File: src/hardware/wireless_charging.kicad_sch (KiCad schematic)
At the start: 0 parts

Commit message: Added Wireless Charging
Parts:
- added C? (x4): 22nF, symbol Device:C
- added C? (x2): 470nF, symbol Device:C
- added C?: 100pF, symbol Device:C
- added C? (x3): 10nF, symbol Device:C
- added C? (x2): 100nF, symbol Device:C
- added C?: 2.2nF, symbol Device:C
- added C?: 10µF, symbol Device:C
- added L?: WE-WPCC_RX_1COIL, WE-WPCC_RX_1COIL:WE-WPCC_RX_760308103205, symbol WE-WPCC_RX_1COIL:WE-WPCC_RX_1COIL
- added Q? (x2): Q_NMOS, symbol Device:Q_NMOS
- added R?: 422, symbol Device:R
- added R?: 1.5k, symbol Device:R
- added R?: 200, symbol Device:R
- added R?: 10k, symbol Device:R
- added U?: BQ51013BRHLR, BQ51013BRHLR:IC_MSP430FR2522IRHLR, symbol BQ51013BRHLR:BQ51013BRHLR
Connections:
- new net: C?.2, C?.2, C?.2, C?.2, L?.1
- new net: R?.1, U?.12 (ILIM)
- new net: R?.1, R?.2, U?.14 (FOD)
- new net: Q?.D, Q?.D
- new net: R?.1, U?.7 (~{CHG})
- new net: R?.1, U?.13 (TS/CTRL)
- new net AC1: C?.1, C?.1, C?.1, C?.1, C?.1, C?.1, C?.2, C?.2, C?.2, U?.2 (AC1)
- new net AC2: C?.2, C?.2, C?.2, C?.2, C?.2, L?.2, U?.18 (RECT), U?.19 (AC2)
- new net BOOT1: C?.1, U?.3 (BOOT1)
- new net BOOT2: C?.1, U?.17 (BOOT2)
- new net CLAMP1: C?.1, U?.5 (CLAMP1)
- new net CLAMP2: C?.1, U?.16 (CLAMP2)
- new net COMM1: C?.1, U?.6 (COMM1)
- new net COMM2: C?.1, U?.15 (COMM2)
- new net EXP: C?.1, C?.1, R?.2, R?.2, U?.1 (PGND), U?.10 (EN1), U?.11 (EN2), U?.20 (PGND), U?.21 (EXP), U?.22 (EXP), U?.23 (EXP), U?.24 (EXP), U?.25 (EXP), U?.26 (EXP), U?.27 (EXP), U?.28 (EXP), U?.29 (EXP)
- new net SOLAR: C?.2, C?.2, Q?.S, U?.9 (AD)
- new net WCDET: R?.2
- new net \ADEN: Q?.G, Q?.G, U?.8 (~{AD}-EN)

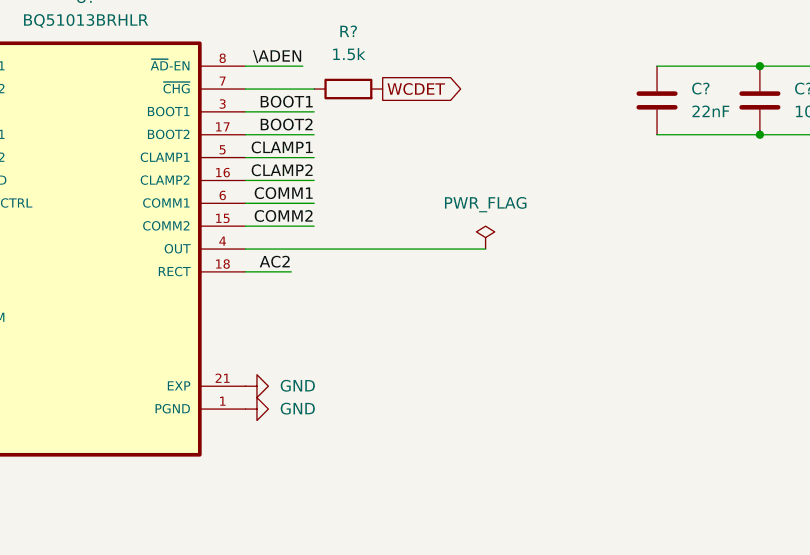
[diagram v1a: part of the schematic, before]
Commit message: Fixed Wireless Charging
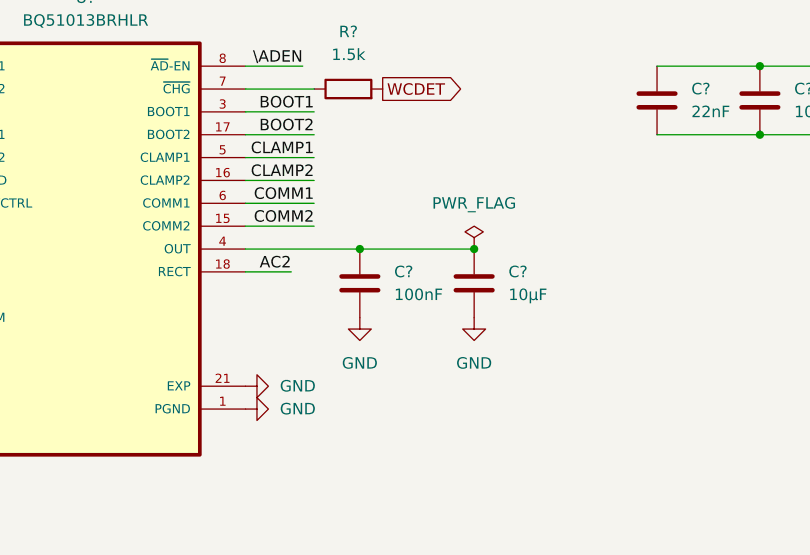
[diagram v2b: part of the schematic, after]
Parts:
- added C?: 100nF, symbol Device:C
- added C?: 10µF, symbol Device:C
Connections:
- net EXP: now also C?.2, C?.2
- net at U?.4 (OUT): now also C?.1, C?.1

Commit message: Added Solar Status
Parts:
- added R6: 10k, symbol Device:R
- R?: value 1.5k -> 10k
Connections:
- net \ADEN: now also R6.1
- new net SOLARSTAT: R6.2
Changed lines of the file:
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@@
+	)
+	(junction
+		(at 161.29 76.2)
+		(diameter 0)
+		(color 0 0 0 0)
 	)
 	(junction
@@
 	(wire
 		(pts
+			(xy 161.29 67.31) (xy 161.29 76.2)
+		)
+		(stroke
+			(width 0)
+			(type default)
+		)
+	)
+	(wire
+		(pts
 			(xy 163.83 85.09) (xy 156.21 85.09)
 		)
@@
 	(wire
 		(pts
+			(xy 161.29 76.2) (xy 161.29 82.55)
+		)
+		(stroke
+			(width 0)
+			(type default)
+		)
+	)
+	(wire
+		(pts
 			(xy 213.36 90.17) (xy 224.79 90.17)
 		)
@@
 	(wire
 		(pts
-			(xy 156.21 82.55) (xy 162.56 82.55)
+			(xy 161.29 67.31) (xy 171.45 67.31)
 		)
 		(stroke
@@
 	(wire
 		(pts
+			(xy 161.29 76.2) (xy 163.83 76.2)
+		)
+		(stroke
+			(width 0)
+			(type default)
+		)
+	)
+	(wire
+		(pts
 			(xy 43.18 105.41) (xy 48.26 105.41)
 		)
@@
 	(wire
 		(pts
+			(xy 161.29 82.55) (xy 156.21 82.55)
+		)
+		(stroke
+			(width 0)
+			(type default)
+		)
+	)
+	(wire
+		(pts
 			(xy 48.26 105.41) (xy 58.42 105.41)
 		)
@@
 	)
 	(label "\\ADEN"
-		(at 162.56 82.55 180)
+		(at 171.45 67.31 180)
 		(effects
 			(font
@@
 		(property "Intersheetrefs" "${INTERSHEET_REFS}"
 			(at 180.5432 85.09 0)
+			(effects
+				(font
+					(size 1.27 1.27)
+				)
+				(justify left)
+				(hide yes)
+			)
+		)
+	)
+	(global_label "SOLARSTAT"
+		(shape output)
+		(at 171.45 76.2 0)
+		(fields_autoplaced yes)
+		(effects
+			(font
+				(size 1.27 1.27)
+			)
+			(justify left)
+		)
+		(property "Intersheetrefs" "${INTERSHEET_REFS}"
+			(at 184.5952 76.2 0)
 			(effects
 				(font
@@
 	)
 	(symbol
+		(lib_id "Device:R")
+		(at 167.64 76.2 90)
+		(unit 1)
+		(exclude_from_sim no)
+		(in_bom yes)
+		(on_board yes)
+		(dnp no)
+		(fields_autoplaced yes)
+		(property "Reference" "R6"
+			(at 167.64 69.85 90)
+			(effects
+				(font
+					(size 1.27 1.27)
+				)
+			)
+		)
+		(property "Value" "10k"
+			(at 167.64 72.39 90)
+			(effects
+				(font
+					(size 1.27 1.27)
+				)
+			)
+		)
+		(property "Footprint" ""
+			(at 167.64 77.978 90)
+			(effects
+				(font
+					(size 1.27 1.27)
+				)
+				(hide yes)
+			)
+		)
+		(property "Datasheet" "~"
+			(at 167.64 76.2 0)
+			(effects
+				(font
+					(size 1.27 1.27)
+				)
+				(hide yes)
+			)
+		)
+		(property "Description" "Resistor"
+			(at 167.64 76.2 0)
+			(effects
+				(font
+					(size 1.27 1.27)
+				)
+				(hide yes)
+			)
+		)
+		(pin "1"
+		)
+		(pin "2"
+		)
+		(instances
+			(project "raywatch"
+				(path "/7b654ee8-2a53-4d39-8b7d-32c7bb3cb0ed/6e6a70ea-4db2-4b59-a2d7-c468f9b8b5a6/d00e072b-2be1-497b-8423-3eead973d996"
+					(reference "R6")
+					(unit 1)
+				)
+			)
+		)
+	)
+	(symbol
 		(lib_id "Device:C")
 		(at 250.19 102.87 270)
@@
 			)
 		)
-		(property "Value" "1.5k"
+		(property "Value" "10k"
 			(at 167.64 81.28 90)
 			(effects

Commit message: Changed power symboles
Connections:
- net VIN: now reaches C?.1, C?.1, U?.4 (OUT)
- net LINE: now reaches Q?.S
- net SOLAR renamed VSOLAR
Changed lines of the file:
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@@
 	)
 	(junction
-		(at 181.61 102.87)
-		(diameter 0)
-		(color 0 0 0 0)
-	)
-	(junction
 		(at 224.79 82.55)
 		(diameter 0)
@@
 		(color 0 0 0 0)
 	)
+	(junction
+		(at 181.61 102.87)
+		(diameter 0)
+		(color 0 0 0 0)
+	)
 	(wire
 		(pts
@@
 	(wire
 		(pts
-			(xy 43.18 102.87) (xy 43.18 105.41)
-		)
-		(stroke
-			(width 0)
-			(type default)
-		)
-	)
-	(wire
-		(pts
 			(xy 66.04 100.33) (xy 72.39 100.33)
 		)
@@
 		)
 	)
-	(global_label "SOLAR"
-		(shape passive)
-		(at 43.18 102.87 90)
-		(fields_autoplaced yes)
-		(effects
-			(font
-				(size 1.27 1.27)
-			)
-			(justify left)
-		)
-		(property "Intersheetrefs" "${INTERSHEET_REFS}"
-			(at 43.18 95.0694 90)
-			(effects
-				(font
-					(size 1.27 1.27)
-				)
-				(justify left)
-				(hide yes)
-			)
-		)
-	)
 	(global_label "WCDET"
 		(shape output)
@@
 	)
 	(symbol
-		(lib_id "power:PWR_FLAG")
+		(lib_id "power:LINE")
 		(at 181.61 102.87 0)
 		(unit 1)
@@
 		(dnp no)
 		(fields_autoplaced yes)
-		(property "Reference" "#FLG02"
-			(at 181.61 100.965 0)
+		(property "Reference" "#PWR0369"
+			(at 181.61 106.68 0)
 			(effects
 				(font
@@
 			)
 		)
-		(property "Value" "PWR_FLAG"
+		(property "Value" "VIN"
 			(at 181.61 97.79 0)
 			(effects
@@
 			)
 		)
-		(property "Datasheet" "~"
+		(property "Datasheet" ""
 			(at 181.61 102.87 0)
 			(effects
@@
 			)
 		)
-		(property "Description" "Special symbol for telling ERC where power comes from"
+		(property "Description" "Power symbol creates a global label with name \"LINE\""
 			(at 181.61 102.87 0)
 			(effects
@@
 			(project "raywatch"
 				(path "/7b654ee8-2a53-4d39-8b7d-32c7bb3cb0ed/6e6a70ea-4db2-4b59-a2d7-c468f9b8b5a6/d00e072b-2be1-497b-8423-3eead973d996"
-					(reference "#FLG02")
+					(reference "#PWR0369")
+					(unit 1)
+				)
+			)
+		)
+	)
+	(symbol
+		(lib_id "power:LINE")
+		(at 43.18 105.41 0)
+		(unit 1)
+		(exclude_from_sim no)
+		(in_bom yes)
+		(on_board yes)
+		(dnp no)
+		(fields_autoplaced yes)
+		(property "Reference" "#PWR0370"
+			(at 43.18 109.22 0)
+			(effects
+				(font
+					(size 1.27 1.27)
+				)
+				(hide yes)
+			)
+		)
+		(property "Value" "VSOLAR"
+			(at 43.18 100.33 0)
+			(effects
+				(font
+					(size 1.27 1.27)
+				)
+			)
+		)
+		(property "Footprint" ""
+			(at 43.18 105.41 0)
+			(effects
+				(font
+					(size 1.27 1.27)
+				)
+				(hide yes)
+			)
+		)
+		(property "Datasheet" ""
+			(at 43.18 105.41 0)
+			(effects
+				(font
+					(size 1.27 1.27)
+				)
+				(hide yes)
+			)
+		)
+		(property "Description" "Power symbol creates a global label with name \"LINE\""
+			(at 43.18 105.41 0)
+			(effects
+				(font
+					(size 1.27 1.27)
+				)
+				(hide yes)
+			)
+		)
+		(pin "1"
+		)
+		(instances
+			(project "raywatch"
+				(path "/7b654ee8-2a53-4d39-8b7d-32c7bb3cb0ed/6e6a70ea-4db2-4b59-a2d7-c468f9b8b5a6/d00e072b-2be1-497b-8423-3eead973d996"
+					(reference "#PWR0370")
 					(unit 1)
 				)
@@
 	)
 	(symbol
+		(lib_id "power:LINE")
+		(at 58.42 85.09 0)
+		(unit 1)
+		(exclude_from_sim no)
+		(in_bom yes)
+		(on_board yes)
+		(dnp no)
+		(fields_autoplaced yes)
+		(property "Reference" "#PWR0368"
+			(at 58.42 88.9 0)
+			(effects
+				(font
+					(size 1.27 1.27)
+				)
+				(hide yes)
+			)
+		)
+		(property "Value" "LINE"
+			(at 58.42 80.01 0)
+			(effects
+				(font
+					(size 1.27 1.27)
+				)
+			)
+		)
+		(property "Footprint" ""
+			(at 58.42 85.09 0)
+			(effects
+				(font
+					(size 1.27 1.27)
+				)
+				(hide yes)
+			)
+		)
+		(property "Datasheet" ""
+			(at 58.42 85.09 0)
+			(effects
+				(font
+					(size 1.27 1.27)
+				)
+				(hide yes)
+			)
+		)
+		(property "Description" "Power symbol creates a global label with name \"LINE\""
+			(at 58.42 85.09 0)
+			(effects
+				(font
+					(size 1.27 1.27)
+				)
+				(hide yes)
+			)
+		)
+		(pin "1"
+		)
+		(instances
+			(project "raywatch"
+				(path "/7b654ee8-2a53-4d39-8b7d-32c7bb3cb0ed/6e6a70ea-4db2-4b59-a2d7-c468f9b8b5a6/d00e072b-2be1-497b-8423-3eead973d996"
+					(reference "#PWR0368")
+					(unit 1)
+				)
+			)
+		)
+	)
+	(symbol
 		(lib_id "Device:Q_NMOS")
 		(at 60.96 100.33 0)
@@
 					(unit 1)
 				)
-			)
-		)
-	)
-	(symbol
-		(lib_id "power:PWR_FLAG")
-		(at 58.42 85.09 0)
-		(unit 1)
-		(exclude_from_sim no)
-		(in_bom yes)
-		(on_board yes)
-		(dnp no)
-		(fields_autoplaced yes)
-		(property "Reference" "#FLG01"
-			(at 58.42 83.185 0)
-			(effects
-				(font
-					(size 1.27 1.27)
-				)
-				(hide yes)
-			)
-		)
-		(property "Value" "PWR_FLAG"
-			(at 58.42 80.01 0)
-			(effects
-				(font
-					(size 1.27 1.27)
-				)
-			)
-		)
-		(property "Footprint" ""
-			(at 58.42 85.09 0)
-			(effects
-				(font
-					(size 1.27 1.27)
-				)
-				(hide yes)
-			)
-		)
-		(property "Datasheet" "~"
-			(at 58.42 85.09 0)
-			(effects
-				(font
-					(size 1.27 1.27)
-				)
-				(hide yes)
-			)
-		)
-		(property "Description" "Special symbol for telling ERC where power comes from"
-			(at 58.42 85.09 0)
-			(effects
-				(font
-					(size 1.27 1.27)
-				)
-				(hide yes)
-			)
-		)
-		(pin "1"
-		)
-		(instances
-			(project "raywatch"
-				(path "/7b654ee8-2a53-4d39-8b7d-32c7bb3cb0ed/6e6a70ea-4db2-4b59-a2d7-c468f9b8b5a6/d00e072b-2be1-497b-8423-3eead973d996"
-					(reference "#FLG01")
-					(unit 1)
-				)

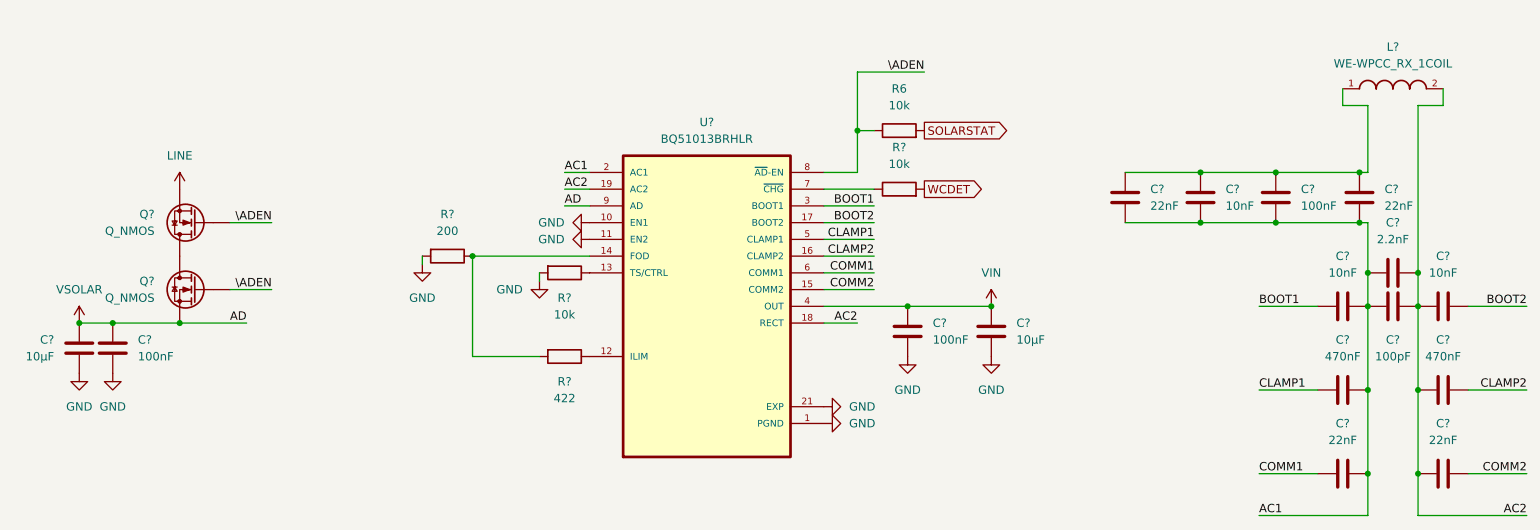
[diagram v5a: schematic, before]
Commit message: Fixed Wireless Charging
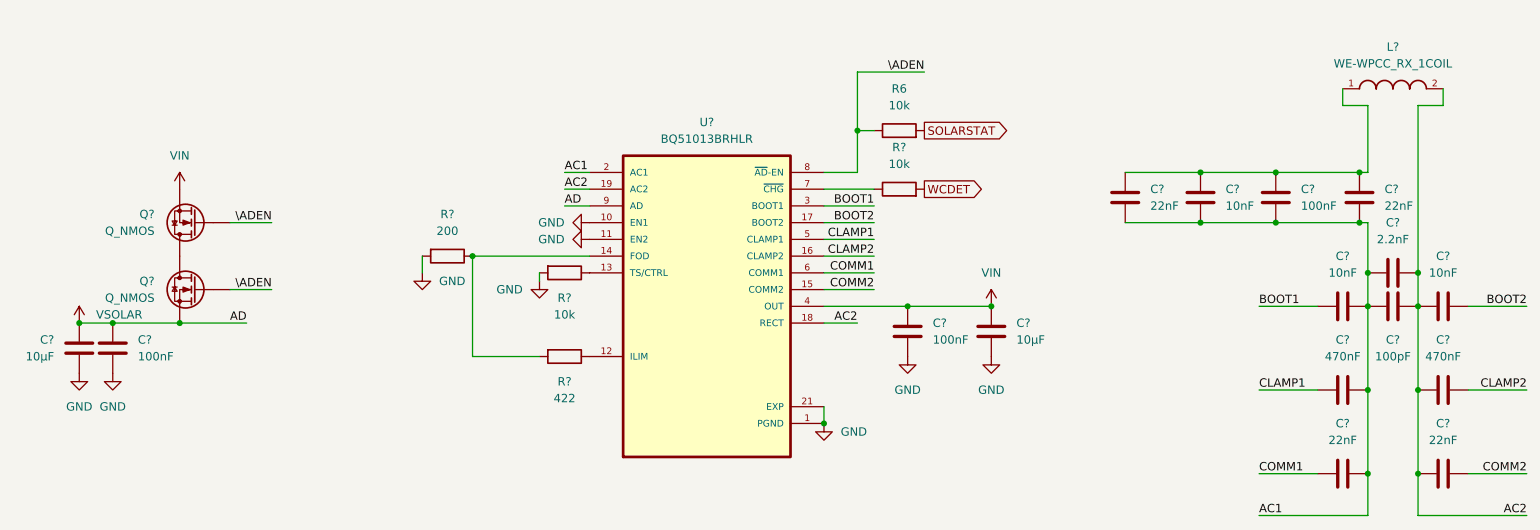
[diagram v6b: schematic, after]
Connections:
- net LINE is gone; now on net VIN: Q?.S
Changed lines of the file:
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@@
 	)
 	(junction
+		(at 156.21 120.65)
+		(diameter 0)
+		(color 0 0 0 0)
+	)
+	(junction
 		(at 224.79 82.55)
 		(diameter 0)
@@
 	(wire
 		(pts
-			(xy 95.25 96.52) (xy 95.25 95.25)
+			(xy 95.25 97.79) (xy 95.25 95.25)
 		)
 		(stroke
@@
 	(wire
 		(pts
+			(xy 156.21 118.11) (xy 156.21 120.65)
+		)
+		(stroke
+			(width 0)
+			(type default)
+		)
+	)
+	(wire
+		(pts
 			(xy 234.95 72.39) (xy 238.76 72.39)
 		)
@@
 	(symbol
 		(lib_id "power:GND")
-		(at 156.21 120.65 90)
+		(at 156.21 120.65 0)
 		(unit 1)
 		(exclude_from_sim no)
@@
 		(fields_autoplaced yes)
 		(property "Reference" "#PWR0341"
-			(at 162.56 120.65 0)
+			(at 156.21 127 0)
 			(effects
 				(font
@@
 		)
 		(property "Value" "GND"
-			(at 160.02 120.6499 90)
+			(at 158.75 121.9199 0)
 			(effects
 				(font
 					(size 1.27 1.27)
 				)
-				(justify right)
+				(justify left)
 			)
 		)
@@
 		)
 		(property "Value" "VSOLAR"
-			(at 43.18 100.33 0)
+			(at 45.72 104.1399 0)
 			(effects
 				(font
 					(size 1.27 1.27)
 				)
+				(justify left)
 			)
 		)
@@
 	)
 	(symbol
-		(lib_id "power:GND")
-		(at 156.21 118.11 90)
-		(unit 1)
-		(exclude_from_sim no)
-		(in_bom yes)
-		(on_board yes)
-		(dnp no)
-		(fields_autoplaced yes)
-		(property "Reference" "#PWR0342"
-			(at 162.56 118.11 0)
-			(effects
-				(font
-					(size 1.27 1.27)
-				)
-				(hide yes)
-			)
-		)
-		(property "Value" "GND"
-			(at 160.02 118.1099 90)
-			(effects
-				(font
-					(size 1.27 1.27)
-				)
-				(justify right)
-			)
-		)
-		(property "Footprint" ""
-			(at 156.21 118.11 0)
-			(effects
-				(font
-					(size 1.27 1.27)
-				)
-				(hide yes)
-			)
-		)
-		(property "Datasheet" ""
-			(at 156.21 118.11 0)
-			(effects
-				(font
-					(size 1.27 1.27)
-				)
-				(hide yes)
-			)
-		)
-		(property "Description" "Power symbol creates a global label with name \"GND\" , ground"
-			(at 156.21 118.11 0)
-			(effects
-				(font
-					(size 1.27 1.27)
-				)
-				(hide yes)
-			)
-		)
-		(pin "1"
-		)
-		(instances
-			(project "raywatch"
-				(path "/7b654ee8-2a53-4d39-8b7d-32c7bb3cb0ed/6e6a70ea-4db2-4b59-a2d7-c468f9b8b5a6/d00e072b-2be1-497b-8423-3eead973d996"
-					(reference "#PWR0342")
-					(unit 1)
-				)
-			)
-		)
-	)
-	(symbol
 		(lib_id "Device:C")
 		(at 181.61 106.68 0)
@@
 			)
 		)
-		(property "Value" "LINE"
+		(property "Value" "VIN"
 			(at 58.42 80.01 0)
 			(effects
@@
 	(symbol
 		(lib_id "power:GND")
-		(at 95.25 96.52 0)
+		(at 95.25 97.79 0)
 		(unit 1)
 		(exclude_from_sim no)
@@
 		(fields_autoplaced yes)
 		(property "Reference" "#PWR0346"
-			(at 95.25 102.87 0)
+			(at 95.25 104.14 0)
 			(effects
 				(font
@@
 		)
 		(property "Value" "GND"
-			(at 95.25 101.6 0)
+			(at 97.79 99.0599 0)
 			(effects
 				(font
 					(size 1.27 1.27)
 				)
+				(justify left)
 			)
 		)
 		(property "Footprint" ""
-			(at 95.25 96.52 0)
+			(at 95.25 97.79 0)
 			(effects
 				(font
@@
 		)
 		(property "Datasheet" ""
-			(at 95.25 96.52 0)
+			(at 95.25 97.79 0)
 			(effects
 				(font
@@
 		)
 		(property "Description" "Power symbol creates a global label with name \"GND\" , ground"
-			(at 95.25 96.52 0)
+			(at 95.25 97.79 0)
 			(effects
 				(font

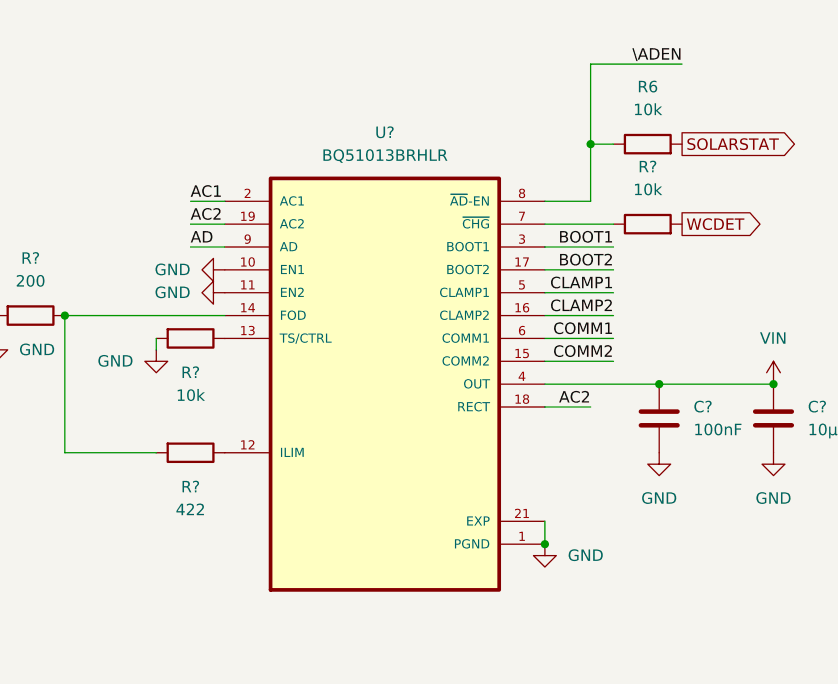
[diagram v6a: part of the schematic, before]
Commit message: Added Accelerometer Clock; Cleanup & Fixes
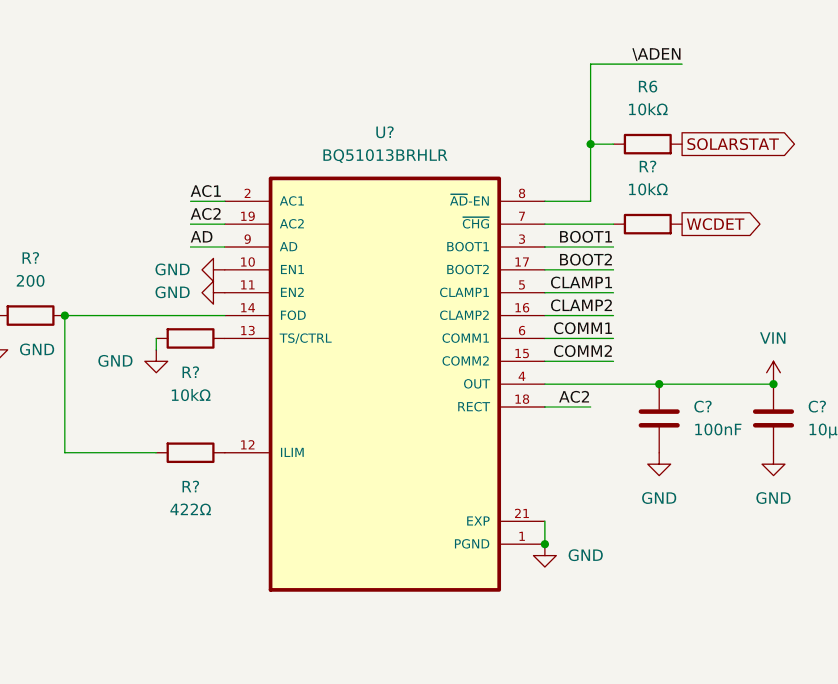
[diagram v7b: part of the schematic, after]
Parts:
- R6, R? (x2): value 10k -> 10kΩ
- R?: value 422 -> 422Ω
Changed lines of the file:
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@@
 			)
 		)
-		(property "Value" "422"
+		(property "Value" "422Ω"
 			(at 116.84 116.84 90)
 			(effects
@@
 			)
 		)
-		(property "Value" "10k"
+		(property "Value" "10kΩ"
 			(at 167.64 72.39 90)
 			(effects
@@
 			)
 		)
-		(property "Value" "10k"
+		(property "Value" "10kΩ"
 			(at 167.64 81.28 90)
 			(effects
@@
 			)
 		)
-		(property "Value" "10k"
+		(property "Value" "10kΩ"
 			(at 116.84 104.14 90)
 			(effects
